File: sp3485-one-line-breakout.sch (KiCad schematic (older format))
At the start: 4 parts, among them J1 Conn_01x08, U1 SP3485CN

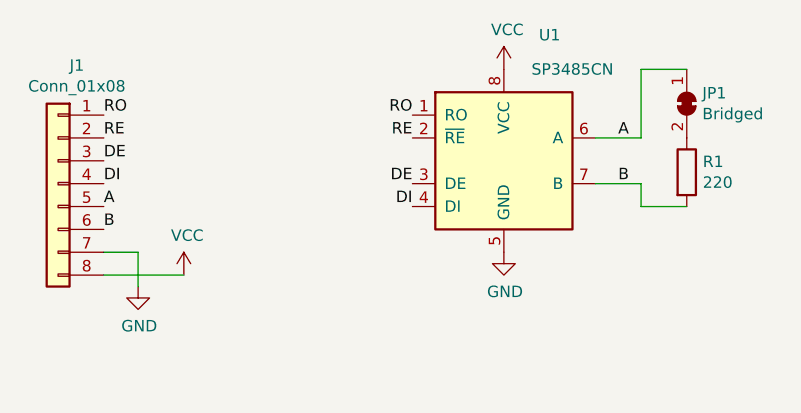
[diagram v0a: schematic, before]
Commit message: Change resistor size and add capacitor
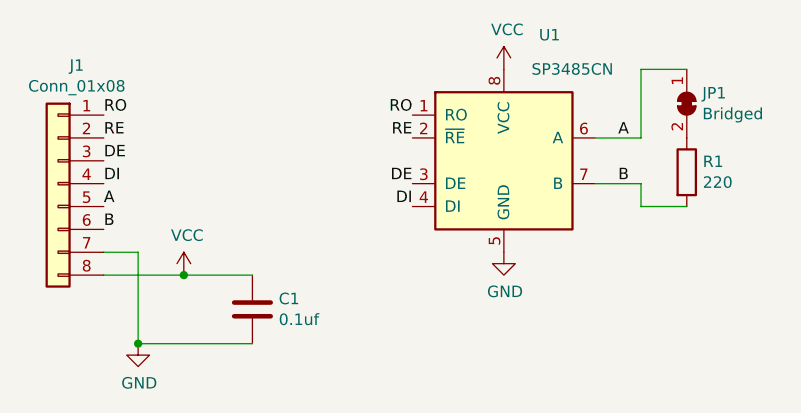
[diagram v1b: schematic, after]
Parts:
- added C1: 0.1uf, Capacitor_SMD:C_0402_1005Metric, symbol Device:C
- R1: footprint Resistor_SMD:R_0603_1608Metric -> Resistor_SMD:R_0402_1005Metric
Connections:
- net GND: now also C1.2
- net VCC: now also C1.1
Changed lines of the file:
@@
 F 0 "R1" H 6870 3346 50  0000 L CNN
 F 1 "220" H 6870 3255 50  0000 L CNN
-F 2 "Resistor_SMD:R_0603_1608Metric" V 6730 3300 50  0001 C CNN
+F 2 "Resistor_SMD:R_0402_1005Metric" V 6730 3300 50  0001 C CNN
 F 3 "~" H 6800 3300 50  0001 C CNN
 	1    6800 3300
@@
 L power:GND #PWR0103
 U 1 1 5F9D5FAB
-P 4400 3800
-F 0 "#PWR0103" H 4400 3550 50  0001 C CNN
-F 1 "GND" H 4405 3627 50  0000 C CNN
-F 2 "" H 4400 3800 50  0001 C CNN
-F 3 "" H 4400 3800 50  0001 C CNN
-	1    4400 3800
+P 4400 4050
+F 0 "#PWR0103" H 4400 3800 50  0001 C CNN
+F 1 "GND" H 4405 3877 50  0000 C CNN
+F 2 "" H 4400 4050 50  0001 C CNN
+F 3 "" H 4400 4050 50  0001 C CNN
+	1    4400 4050
 	1    0    0    -1
 $EndComp
@@
 	4600 3750 4250 3750
 Wire Wire Line
-	4400 3800 4400 3650
-Wire Wire Line
 	4400 3650 4250 3650
 Text Label 4250 3550 0    50   ~ 0
@@
 Text Label 4250 3350 0    50   ~ 0
 DI
+$Comp
+L Device:C C1
+U 1 1 608E489F
+P 4900 3900
+F 0 "C1" H 5015 3946 50  0000 L CNN
+F 1 "0.1uf" H 5015 3855 50  0000 L CNN
+F 2 "Capacitor_SMD:C_0402_1005Metric" H 4938 3750 50  0001 C CNN
+F 3 "~" H 4900 3900 50  0001 C CNN
+	1    4900 3900
+	1    0    0    -1
+$EndComp
+Wire Wire Line
+	4600 3750 4900 3750
+Connection ~ 4600 3750
+Wire Wire Line
+	4400 4050 4900 4050
+Wire Wire Line
+	4400 3650 4400 4050
+Connection ~ 4400 4050
 $EndSCHEMATC
